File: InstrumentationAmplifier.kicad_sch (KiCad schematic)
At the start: 2 parts, among them U1 INA115BU

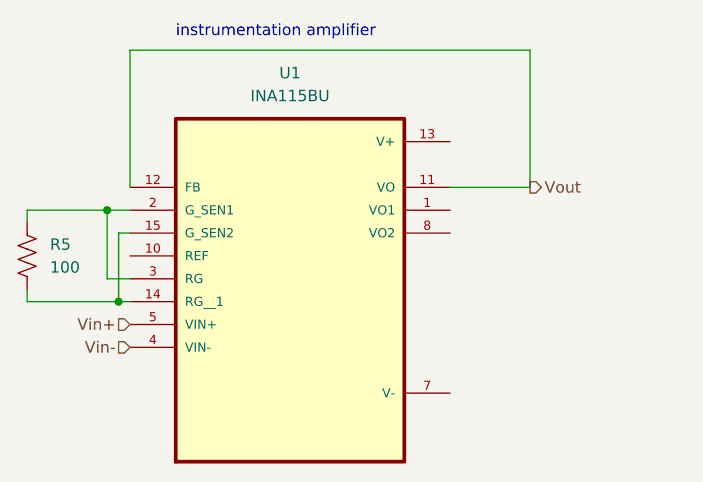
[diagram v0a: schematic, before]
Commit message: swapped lpf and hpf in bandpass filter and added testpoints on various filter circuits
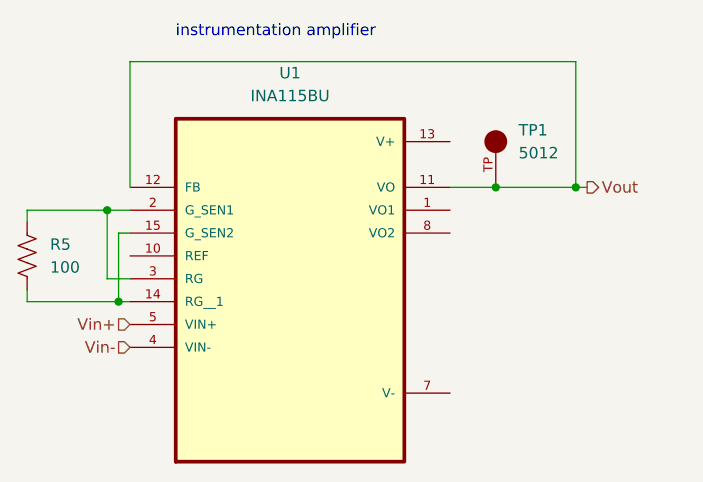
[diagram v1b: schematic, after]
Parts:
- added TP1: 5012, 5012:TP_5012, symbol TP_5012:5012
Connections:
- net Vout: now also TP1.TP
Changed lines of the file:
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@@
   (junction (at 118.11 85.09) (diameter 0) (color 0 0 0 0)
   )
-  (wire (pts (xy 154.94 72.39) (xy 163.83 72.39))
-    (stroke (width 0) (type default))
+  (junction (at 168.91 72.39) (diameter 0) (color 0 0 0 0)
   )
-  (wire (pts (xy 163.83 72.39) (xy 163.83 57.15))
+  (junction (at 160.02 72.39) (diameter 0) (color 0 0 0 0)
+  )
+  (wire (pts (xy 154.94 72.39) (xy 160.02 72.39))
     (stroke (width 0) (type default))
   )
@@
     (stroke (width 0) (type default))
   )
-  (wire (pts (xy 119.38 57.15) (xy 119.38 72.39))
+  (wire (pts (xy 119.38 58.42) (xy 119.38 72.39))
+    (stroke (width 0) (type default))
+  )
+  (wire (pts (xy 119.38 58.42) (xy 168.91 58.42))
     (stroke (width 0) (type default))
   )
@@
     (stroke (width 0) (type default))
   )
-  (wire (pts (xy 163.83 57.15) (xy 119.38 57.15))
+  (wire (pts (xy 168.91 72.39) (xy 170.18 72.39))
     (stroke (width 0) (type default))
   )
@@
   )
   (wire (pts (xy 107.95 85.09) (xy 118.11 85.09))
+    (stroke (width 0) (type default))
+  )
+  (wire (pts (xy 160.02 72.39) (xy 168.91 72.39))
+    (stroke (width 0) (type default))
+  )
+  (wire (pts (xy 168.91 58.42) (xy 168.91 72.39))
     (stroke (width 0) (type default))
   )
@@
     (effects (font (size 1.27 1.27)) (justify left bottom))
   )
-  (hierarchical_label "Vout" (shape output) (at 163.83 72.39 0) (fields_autoplaced)
+  (hierarchical_label "Vout" (shape output) (at 170.18 72.39 0) (fields_autoplaced)
     (effects (font (size 1.27 1.27)) (justify left))
   )
@@
         )
       )
+    )
+  )
+  (symbol (lib_id "TP_5012:5012") (at 160.02 67.31 90) (unit 1)
+    (in_bom yes) (on_board yes) (dnp no) (fields_autoplaced)
+    (property "Reference" "TP1" (at 162.56 66.04 90)
+      (effects (font (size 1.27 1.27)) (justify right))
+    )
+    (property "Value" "5012" (at 162.56 68.58 90)
+      (effects (font (size 1.27 1.27)) (justify right))
+    )
+    (property "Footprint" "5012:TP_5012" (at 160.02 67.31 0)
+      (effects (font (size 1.27 1.27)) (justify bottom) hide)
+    )
+    (property "Datasheet" "" (at 160.02 67.31 0)
+      (effects (font (size 1.27 1.27)) hide)
+    )
+    (property "PARTREV" "F" (at 160.02 67.31 0)
+      (effects (font (size 1.27 1.27)) (justify bottom) hide)
+    )
+    (property "SNAPEDA_PN" "5010" (at 160.02 67.31 0)
+      (effects (font (size 1.27 1.27)) (justify bottom) hide)
+    )
+    (property "MANUFACTURER" "Keystone Electronics" (at 160.02 67.31 0)
+      (effects (font (size 1.27 1.27)) (justify bottom) hide)
+    )
+    (property "MAXIMUM_PACKAGE_HEIGHT" "8.13 mm" (at 160.02 67.31 0)
+      (effects (font (size 1.27 1.27)) (justify bottom) hide)
+    )
+    (property "STANDARD" "Manufacturer Recommendations" (at 160.02 67.31 0)
+      (effects (font (size 1.27 1.27)) (justify bottom) hide)
+    )
+    (pin "TP")
+    (instances
+      (project "TR_EMG"
+        (path "/c6167f6f-8a8c-40a1-9c06-7f0e8ea44639/59ee8f59-770d-4fda-92bb-823e819fc8fa"
+          (reference "TP1") (unit 1)
+        )
+      )

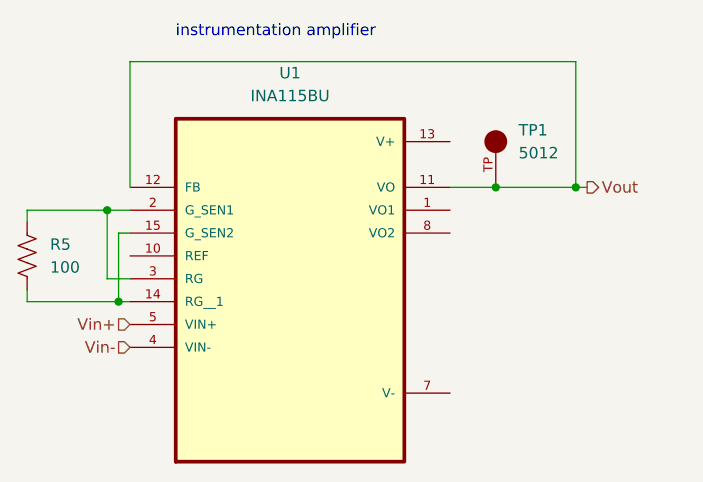
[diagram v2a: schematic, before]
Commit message: Filter abstraction and Input output connectors
Abstracted filters so there are 4 signal paths to go to ADC. Added input and output connectors.
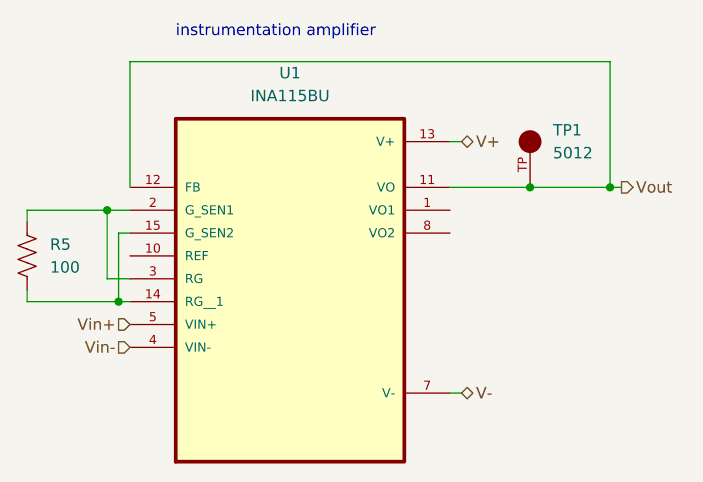
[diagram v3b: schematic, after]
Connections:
- net V+: now reaches U1.13 (V+)
- net V-: now reaches U1.7 (V-)
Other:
- moved on the sheet: TP1
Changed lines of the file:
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@@
   (junction (at 118.11 85.09) (diameter 0) (color 0 0 0 0)
   )
-  (junction (at 168.91 72.39) (diameter 0) (color 0 0 0 0)
+  (junction (at 172.72 72.39) (diameter 0) (color 0 0 0 0)
   )
-  (junction (at 160.02 72.39) (diameter 0) (color 0 0 0 0)
+  (junction (at 163.83 72.39) (diameter 0) (color 0 0 0 0)
   )
-  (wire (pts (xy 154.94 72.39) (xy 160.02 72.39))
+  (wire (pts (xy 154.94 72.39) (xy 163.83 72.39))
     (stroke (width 0) (type default))
   )
   (wire (pts (xy 118.11 85.09) (xy 119.38 85.09))
-    (stroke (width 0) (type default))
-  )
-  (wire (pts (xy 119.38 58.42) (xy 119.38 72.39))
-    (stroke (width 0) (type default))
-  )
-  (wire (pts (xy 119.38 58.42) (xy 168.91 58.42))
     (stroke (width 0) (type default))
   )
@@
     (stroke (width 0) (type default))
   )
-  (wire (pts (xy 168.91 72.39) (xy 170.18 72.39))
+  (wire (pts (xy 172.72 72.39) (xy 173.99 72.39))
     (stroke (width 0) (type default))
   )
@@
     (stroke (width 0) (type default))
   )
+  (wire (pts (xy 154.94 67.31) (xy 156.21 67.31))
+    (stroke (width 0) (type default))
+  )
   (wire (pts (xy 107.95 85.09) (xy 118.11 85.09))
     (stroke (width 0) (type default))
   )
-  (wire (pts (xy 160.02 72.39) (xy 168.91 72.39))
+  (wire (pts (xy 154.94 95.25) (xy 156.21 95.25))
     (stroke (width 0) (type default))
   )
-  (wire (pts (xy 168.91 58.42) (xy 168.91 72.39))
+  (wire (pts (xy 163.83 72.39) (xy 172.72 72.39))
+    (stroke (width 0) (type default))
+  )
+  (wire (pts (xy 172.72 58.42) (xy 172.72 72.39))
+    (stroke (width 0) (type default))
+  )
+  (wire (pts (xy 119.38 58.42) (xy 119.38 72.39))
     (stroke (width 0) (type default))
   )
   (wire (pts (xy 116.84 74.93) (xy 119.38 74.93))
+    (stroke (width 0) (type default))
+  )
+  (wire (pts (xy 119.38 58.42) (xy 172.72 58.42))
     (stroke (width 0) (type default))
   )
@@
     (effects (font (size 1.27 1.27)) (justify left bottom))
   )
-  (hierarchical_label "Vout" (shape output) (at 170.18 72.39 0) (fields_autoplaced)
+  (hierarchical_label "V-" (shape bidirectional) (at 156.21 95.25 0) (fields_autoplaced)
+    (effects (font (size 1.27 1.27)) (justify left))
+  )
+  (hierarchical_label "V+" (shape bidirectional) (at 156.21 67.31 0) (fields_autoplaced)
+    (effects (font (size 1.27 1.27)) (justify left))
+  )
+  (hierarchical_label "Vout" (shape output) (at 173.99 72.39 0) (fields_autoplaced)
     (effects (font (size 1.27 1.27)) (justify left))
   )
@@
     (instances
       (project "TR_EMG"
-        (path "/c6167f6f-8a8c-40a1-9c06-7f0e8ea44639/59ee8f59-770d-4fda-92bb-823e819fc8fa"
+        (path "/c6167f6f-8a8c-40a1-9c06-7f0e8ea44639/e619882c-69e2-4357-9513-12f0ec23e799/bcbf3922-6d95-4131-9e90-9856243d7ce3"
+          (reference "R5") (unit 1)
+        )
+        (path "/c6167f6f-8a8c-40a1-9c06-7f0e8ea44639/a0268632-eb9a-430e-97ab-e20adbf6cd41/bcbf3922-6d95-4131-9e90-9856243d7ce3"
+          (reference "R5") (unit 1)
+        )
+        (path "/c6167f6f-8a8c-40a1-9c06-7f0e8ea44639/1e802adc-784c-4bfc-ac56-2ca34eafc640/bcbf3922-6d95-4131-9e90-9856243d7ce3"
           (reference "R5") (unit 1)
         )
@@
     )
   )
-  (symbol (lib_id "TP_5012:5012") (at 160.02 67.31 90) (unit 1)
+  (symbol (lib_id "TP_5012:5012") (at 163.83 67.31 90) (unit 1)
     (in_bom yes) (on_board yes) (dnp no) (fields_autoplaced)
-    (property "Reference" "TP1" (at 162.56 66.04 90)
+    (property "Reference" "TP1" (at 166.37 66.04 90)
       (effects (font (size 1.27 1.27)) (justify right))
     )
-    (property "Value" "5012" (at 162.56 68.58 90)
+    (property "Value" "5012" (at 166.37 68.58 90)
       (effects (font (size 1.27 1.27)) (justify right))
     )
-    (property "Footprint" "5012:TP_5012" (at 160.02 67.31 0)
+    (property "Footprint" "5012:TP_5012" (at 163.83 67.31 0)
       (effects (font (size 1.27 1.27)) (justify bottom) hide)
     )
-    (property "Datasheet" "" (at 160.02 67.31 0)
+    (property "Datasheet" "" (at 163.83 67.31 0)
       (effects (font (size 1.27 1.27)) hide)
     )
-    (property "PARTREV" "F" (at 160.02 67.31 0)
+    (property "PARTREV" "F" (at 163.83 67.31 0)
       (effects (font (size 1.27 1.27)) (justify bottom) hide)
     )
-    (property "SNAPEDA_PN" "5010" (at 160.02 67.31 0)
+    (property "SNAPEDA_PN" "5010" (at 163.83 67.31 0)
       (effects (font (size 1.27 1.27)) (justify bottom) hide)
     )
-    (property "MANUFACTURER" "Keystone Electronics" (at 160.02 67.31 0)
+    (property "MANUFACTURER" "Keystone Electronics" (at 163.83 67.31 0)
       (effects (font (size 1.27 1.27)) (justify bottom) hide)
     )
-    (property "MAXIMUM_PACKAGE_HEIGHT" "8.13 mm" (at 160.02 67.31 0)
+    (property "MAXIMUM_PACKAGE_HEIGHT" "8.13 mm" (at 163.83 67.31 0)
       (effects (font (size 1.27 1.27)) (justify bottom) hide)
     )
-    (property "STANDARD" "Manufacturer Recommendations" (at 160.02 67.31 0)
+    (property "STANDARD" "Manufacturer Recommendations" (at 163.83 67.31 0)
       (effects (font (size 1.27 1.27)) (justify bottom) hide)
     )
@@
     (instances
       (project "TR_EMG"
-        (path "/c6167f6f-8a8c-40a1-9c06-7f0e8ea44639/59ee8f59-770d-4fda-92bb-823e819fc8fa"
+        (path "/c6167f6f-8a8c-40a1-9c06-7f0e8ea44639/e619882c-69e2-4357-9513-12f0ec23e799/bcbf3922-6d95-4131-9e90-9856243d7ce3"
+          (reference "TP1") (unit 1)
+        )
+        (path "/c6167f6f-8a8c-40a1-9c06-7f0e8ea44639/a0268632-eb9a-430e-97ab-e20adbf6cd41/bcbf3922-6d95-4131-9e90-9856243d7ce3"
+          (reference "TP1") (unit 1)
+        )
+        (path "/c6167f6f-8a8c-40a1-9c06-7f0e8ea44639/1e802adc-784c-4bfc-ac56-2ca34eafc640/bcbf3922-6d95-4131-9e90-9856243d7ce3"
           (reference "TP1") (unit 1)
         )
@@
     (instances
       (project "TR_EMG"
-        (path "/c6167f6f-8a8c-40a1-9c06-7f0e8ea44639/59ee8f59-770d-4fda-92bb-823e819fc8fa"
+        (path "/c6167f6f-8a8c-40a1-9c06-7f0e8ea44639/a0268632-eb9a-430e-97ab-e20adbf6cd41/bcbf3922-6d95-4131-9e90-9856243d7ce3"
           (reference "U1") (unit 1)
         )
+        (path "/c6167f6f-8a8c-40a1-9c06-7f0e8ea44639/fca8234f-eea0-4615-81d1-2ac2d4337d1e/bcbf3922-6d95-4131-9e90-9856243d7ce3"
+          (reference "U1") (unit 1)
+        )
+        (path "/c6167f6f-8a8c-40a1-9c06-7f0e8ea44639/1e802adc-784c-4bfc-ac56-2ca34eafc640/bcbf3922-6d95-4131-9e90-9856243d7ce3"
+          (reference "U1") (unit 1)
+        )
+        (path "/c6167f6f-8a8c-40a1-9c06-7f0e8ea44639/e619882c-69e2-4357-9513-12f0ec23e799/bcbf3922-6d95-4131-9e90-9856243d7ce3"
+          (reference "U1") (unit 1)
+        )

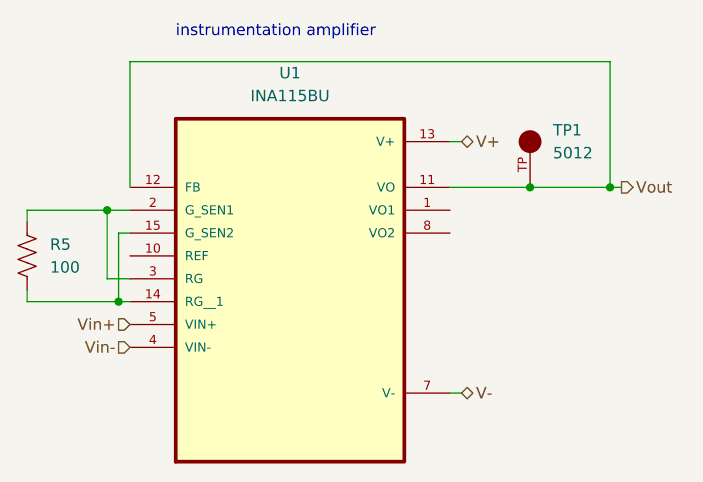
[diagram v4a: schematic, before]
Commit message: Reference Designator and Footprint Updates
Changed almost all reference designators to group similar components by what filter they are a part of and what value they have.

Need to:
- Sort symbol data for ADC and OpAmps to correct folders
- get footprint files for ADC and OpAmps
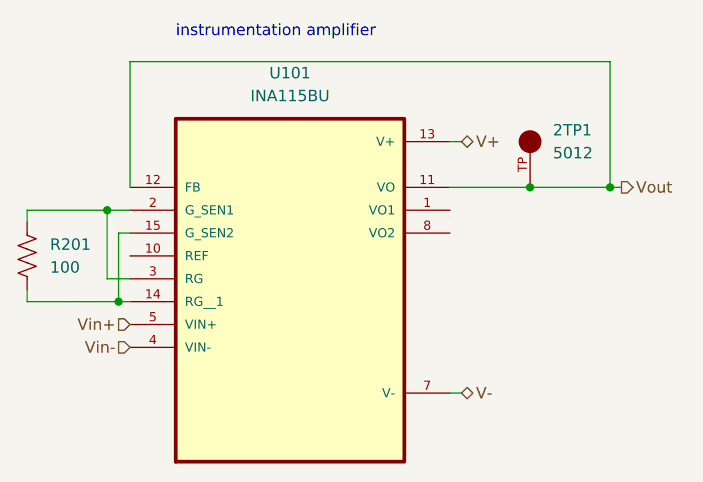
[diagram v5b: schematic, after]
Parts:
- 2TP1: renamed from TP1; footprint 5012:TP_5012 -> footprints:TP_5012
- R201: renamed from R5; footprint (none) -> Resistor_SMD:R_0603_1608Metric_Pad0.98x0.95mm_HandSolder
- U101: renamed from U1; footprint INA115BU:SOIC127P1030X265-16N -> footprints:SOIC127P1030X265-16N
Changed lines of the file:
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@@
   (symbol (lib_id "Device:R_US") (at 107.95 80.01 0) (unit 1)
     (in_bom yes) (on_board yes) (dnp no) (fields_autoplaced)
-    (property "Reference" "R5" (at 110.49 78.74 0)
+    (property "Reference" "R201" (at 110.49 78.74 0)
       (effects (font (size 1.27 1.27)) (justify left))
     )
@@
       (effects (font (size 1.27 1.27)) (justify left))
     )
-    (property "Footprint" "" (at 108.966 80.264 90)
+    (property "Footprint" "Resistor_SMD:R_0603_1608Metric_Pad0.98x0.95mm_HandSolder" (at 108.966 80.264 90)
       (effects (font (size 1.27 1.27)) hide)
     )
@@
       (project "TR_EMG"
         (path "/c6167f6f-8a8c-40a1-9c06-7f0e8ea44639/e619882c-69e2-4357-9513-12f0ec23e799/bcbf3922-6d95-4131-9e90-9856243d7ce3"
-          (reference "R5") (unit 1)
+          (reference "R201") (unit 1)
         )
         (path "/c6167f6f-8a8c-40a1-9c06-7f0e8ea44639/a0268632-eb9a-430e-97ab-e20adbf6cd41/bcbf3922-6d95-4131-9e90-9856243d7ce3"
-          (reference "R5") (unit 1)
+          (reference "R101") (unit 1)
         )
         (path "/c6167f6f-8a8c-40a1-9c06-7f0e8ea44639/1e802adc-784c-4bfc-ac56-2ca34eafc640/bcbf3922-6d95-4131-9e90-9856243d7ce3"
-          (reference "R5") (unit 1)
+          (reference "R301") (unit 1)
         )
         (path "/c6167f6f-8a8c-40a1-9c06-7f0e8ea44639/fca8234f-eea0-4615-81d1-2ac2d4337d1e/bcbf3922-6d95-4131-9e90-9856243d7ce3"
-          (reference "R5") (unit 1)
+          (reference "R401") (unit 1)
         )
       )
@@
   (symbol (lib_id "TP_5012:5012") (at 163.83 67.31 90) (unit 1)
     (in_bom yes) (on_board yes) (dnp no) (fields_autoplaced)
-    (property "Reference" "TP1" (at 166.37 66.04 90)
+    (property "Reference" "2TP1" (at 166.37 66.04 90)
       (effects (font (size 1.27 1.27)) (justify right))
     )
@@
       (effects (font (size 1.27 1.27)) (justify right))
     )
-    (property "Footprint" "5012:TP_5012" (at 163.83 67.31 0)
+    (property "Footprint" "footprints:TP_5012" (at 163.83 67.31 0)
       (effects (font (size 1.27 1.27)) (justify bottom) hide)
     )
@@
       (project "TR_EMG"
         (path "/c6167f6f-8a8c-40a1-9c06-7f0e8ea44639/e619882c-69e2-4357-9513-12f0ec23e799/bcbf3922-6d95-4131-9e90-9856243d7ce3"
-          (reference "TP1") (unit 1)
+          (reference "2TP1") (unit 1)
         )
         (path "/c6167f6f-8a8c-40a1-9c06-7f0e8ea44639/a0268632-eb9a-430e-97ab-e20adbf6cd41/bcbf3922-6d95-4131-9e90-9856243d7ce3"
-          (reference "TP1") (unit 1)
+          (reference "1TP1") (unit 1)
         )
         (path "/c6167f6f-8a8c-40a1-9c06-7f0e8ea44639/1e802adc-784c-4bfc-ac56-2ca34eafc640/bcbf3922-6d95-4131-9e90-9856243d7ce3"
-          (reference "TP1") (unit 1)
+          (reference "3TP1") (unit 1)
         )
         (path "/c6167f6f-8a8c-40a1-9c06-7f0e8ea44639/fca8234f-eea0-4615-81d1-2ac2d4337d1e/bcbf3922-6d95-4131-9e90-9856243d7ce3"
-          (reference "TP1") (unit 1)
+          (reference "4TP1") (unit 1)
         )
       )
@@
   (symbol (lib_id "Digikey:INA115BU") (at 137.16 82.55 0) (unit 1)
     (in_bom yes) (on_board yes) (dnp no) (fields_autoplaced)
-    (property "Reference" "U1" (at 137.16 59.69 0)
+    (property "Reference" "U101" (at 137.16 59.69 0)
       (effects (font (size 1.27 1.27)))
     )
@@
       (effects (font (size 1.27 1.27)))
     )
-    (property "Footprint" "INA115BU:SOIC127P1030X265-16N" (at 137.16 82.55 0)
+    (property "Footprint" "footprints:SOIC127P1030X265-16N" (at 137.16 82.55 0)
       (effects (font (size 1.27 1.27)) (justify bottom) hide)
     )
@@
       (project "TR_EMG"
         (path "/c6167f6f-8a8c-40a1-9c06-7f0e8ea44639/a0268632-eb9a-430e-97ab-e20adbf6cd41/bcbf3922-6d95-4131-9e90-9856243d7ce3"
-          (reference "U1") (unit 1)
+          (reference "U101") (unit 1)
         )
         (path "/c6167f6f-8a8c-40a1-9c06-7f0e8ea44639/fca8234f-eea0-4615-81d1-2ac2d4337d1e/bcbf3922-6d95-4131-9e90-9856243d7ce3"
-          (reference "U1") (unit 1)
+          (reference "U401") (unit 1)
         )
         (path "/c6167f6f-8a8c-40a1-9c06-7f0e8ea44639/1e802adc-784c-4bfc-ac56-2ca34eafc640/bcbf3922-6d95-4131-9e90-9856243d7ce3"
-          (reference "U1") (unit 1)
+          (reference "U301") (unit 1)
         )
         (path "/c6167f6f-8a8c-40a1-9c06-7f0e8ea44639/e619882c-69e2-4357-9513-12f0ec23e799/bcbf3922-6d95-4131-9e90-9856243d7ce3"
-          (reference "U1") (unit 1)
+          (reference "U201") (unit 1)
         )
       )

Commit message: renamed and relinked footprints with better clarity footprint file names
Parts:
- U101: footprint footprints:SOIC127P1030X265-16N -> footprints:INA-SOIC127P1030X265-16N
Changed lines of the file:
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@@
       (effects (font (size 1.27 1.27)))
     )
-    (property "Footprint" "footprints:SOIC127P1030X265-16N" (at 137.16 82.55 0)
+    (property "Footprint" "footprints:INA-SOIC127P1030X265-16N" (at 137.16 82.55 0)
       (effects (font (size 1.27 1.27)) (justify bottom) hide)
     )

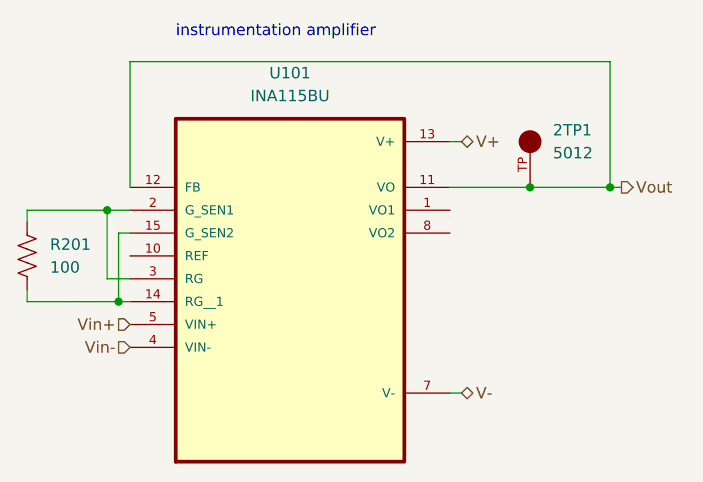
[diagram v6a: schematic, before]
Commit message: first chunk of pcb layout and schematics mods (no connects on pins and changing global labels to hieracarchical labels), one filtering pcb circuit layed out
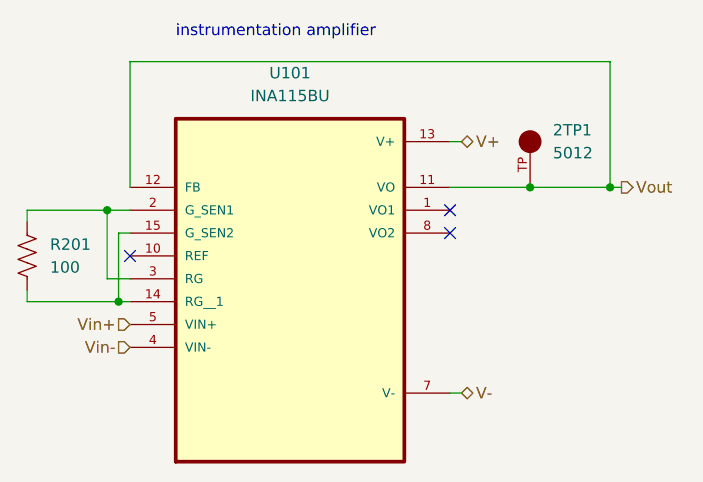
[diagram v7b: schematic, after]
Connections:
- no-connect marks 0 -> 3
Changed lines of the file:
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@@
   (junction (at 163.83 72.39) (diameter 0) (color 0 0 0 0)
   )
+  (no_connect (at 154.94 77.47))
+  (no_connect (at 119.38 80.01))
+  (no_connect (at 154.94 74.93))
   (wire (pts (xy 154.94 72.39) (xy 163.83 72.39))
     (stroke (width 0) (type default))

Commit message: ToTheEdge,LCSCNums
Moved the 3.5mm connectors to the edge and edited their footprint courtyard so no errors. Adjusted the planes so that it bordered 3.5mm connector pads well and didn't go to edge cuts. Added LCSC part numbers to the parts that were in stock.
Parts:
- 2TP1: LCSC (none) -> C238122
- R201: LCSC (none) -> C705888
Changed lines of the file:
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@@
+      (effects (font (size 1.27 1.27)) hide)
+    )
+    (property "LCSC" "C705888" (at 107.95 80.01 0)
       (effects (font (size 1.27 1.27)) hide)
     )
@@
       (effects (font (size 1.27 1.27)) (justify bottom) hide)
     )
+    (property "LCSC" "C238122" (at 163.83 67.31 0)
+      (effects (font (size 1.27 1.27)) hide)
+    )
     (pin "TP")
     (instances
@@
       (effects (font (size 1.27 1.27)) hide)
     )
+    (property "LCSC" "" (at 137.16 82.55 0)
+      (effects (font (size 1.27 1.27)) hide)
+    )
